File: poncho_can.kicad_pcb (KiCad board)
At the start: 2 copper layers, 85.7 x 60.3 mm, 5 parts

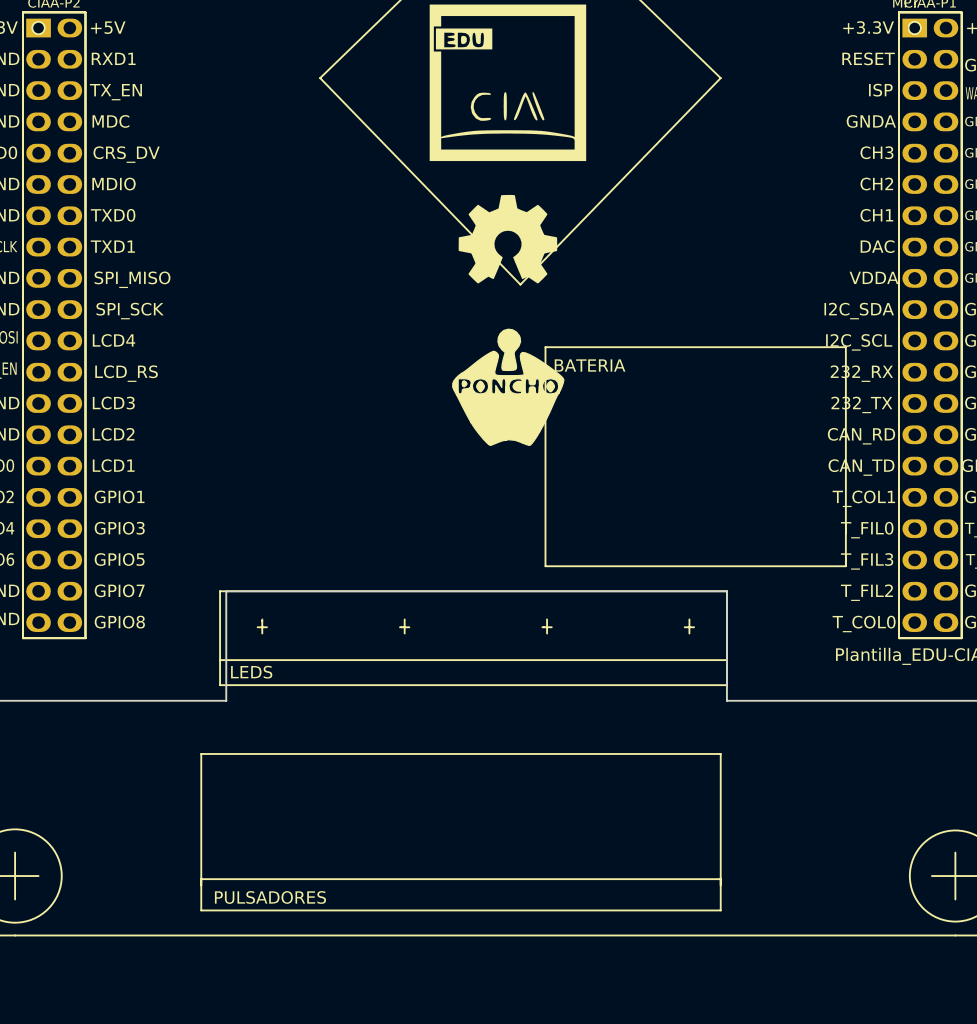
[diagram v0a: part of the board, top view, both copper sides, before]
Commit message: Selección de footprints y ubicacion de componentes
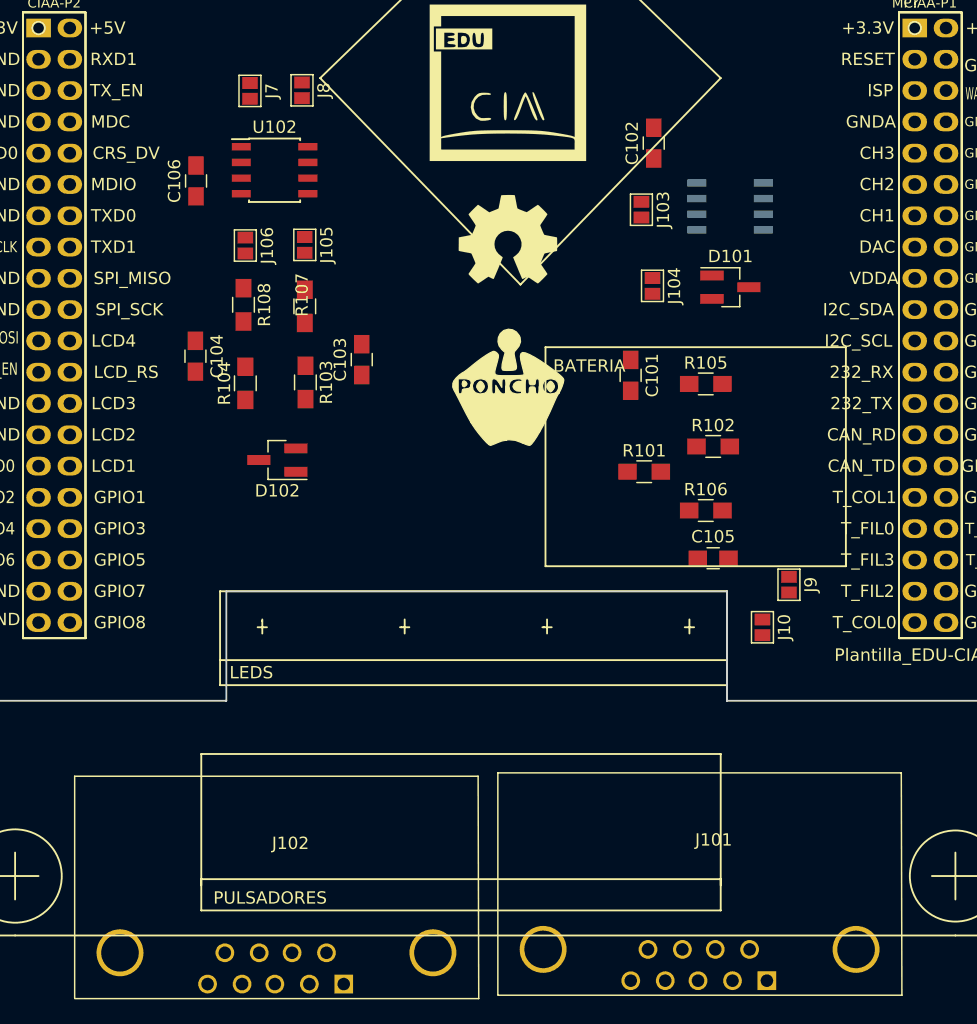
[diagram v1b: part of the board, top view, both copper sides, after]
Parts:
- added C101: 47n, Capacitors_SMD:C_0805_HandSoldering, F.Cu at (114.1, 114.5)
- added C102: 47n, Capacitors_SMD:C_0805_HandSoldering, F.Cu at (116.0, 95.7)
- added C103: 47n, Capacitors_SMD:C_0805_HandSoldering, F.Cu at (92.3, 113.3)
- added C104: 47n, Capacitors_SMD:C_0805_HandSoldering, F.Cu at (78.8, 113.0)
- added C105: 100n, Capacitors_SMD:C_0805_HandSoldering, F.Cu at (120.8, 129.4)
- added C106: 100n, Capacitors_SMD:C_0805_HandSoldering, F.Cu at (78.8, 98.8)
- added D101: RSB27C2, TO_SOT_Packages_SMD:SOT-23_Handsoldering, F.Cu at (122.2, 107.4)
- added D102: RSB27C2, TO_SOT_Packages_SMD:SOT-23_Handsoldering, F.Cu at (85.4, 121.4)
- added J10: GS2, Connect:GS2, F.Cu at (124.8, 135.0)
- added J101: DB9_Male_MountingHoles, Connect:DB9MC, F.Cu at (125.2, 163.7)
- added J102: DB9_Male_MountingHoles, Connect:DB9MC, F.Cu at (90.8, 164.0)
- added J103: GS2, Connect:GS2, F.Cu at (115.0, 101.1)
- added J104: GS2, Connect:GS2, F.Cu at (115.9, 107.3)
- added J105: GS2, Connect:GS2, F.Cu at (87.7, 104.0)
- added J106: GS2, Connect:GS2, F.Cu at (82.8, 104.0)
- added J7: GS2, Connect:GS2, F.Cu at (83.2, 91.5)
- added J8: GS2, Connect:GS2, F.Cu at (87.4, 91.4)
- added J9: GS2, Connect:GS2, F.Cu at (127.0, 131.6)
- added R101: 60, Resistors_SMD:R_0805_HandSoldering, F.Cu at (115.2, 122.4)
- added R102: 60, Resistors_SMD:R_0805_HandSoldering, F.Cu at (120.8, 120.3)
- added R103: 60, Resistors_SMD:R_0805_HandSoldering, F.Cu at (87.7, 115.1)
- added R104: 60, Resistors_SMD:R_0805_HandSoldering, F.Cu at (82.8, 115.2)
- added R105: 60, Resistors_SMD:R_0805_HandSoldering, F.Cu at (120.2, 115.2)
- added R106: 60, Resistors_SMD:R_0805_HandSoldering, F.Cu at (120.2, 125.5)
- added R107: 60, Resistors_SMD:R_0805_HandSoldering, F.Cu at (87.7, 109.0)
- added R108: 60, Resistors_SMD:R_0805_HandSoldering, F.Cu at (82.7, 108.8)
- added U101: TJA1051T, Housings_SOIC:SOIC-8_3.9x4.9mm_Pitch1.27mm, B.Cu at (122.2, 100.8)
- added U102: TJA1051T, Housings_SOIC:SOIC-8_3.9x4.9mm_Pitch1.27mm, F.Cu at (85.2, 97.9)
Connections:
- XA101 pad 1: +3.3VP -> +3V3
- XA101 pad 42: +5V -> +5VP
- XA101 pad 43: GND -> GNDD
- XA101 pad 45: GND -> GNDD
- XA101 pad 47: GND -> GNDD
- XA101 pad 51: GND -> GNDD
- XA101 pad 53: GND -> GNDD
- XA101 pad 57: GND -> GNDD
- XA101 pad 59: GND -> GNDD
- XA101 pad 65: GND -> GNDD
- XA101 pad 67: GND -> GNDD
- XA101 pad 77: GND -> GNDD
- XA101 pad 79: GND -> GNDD

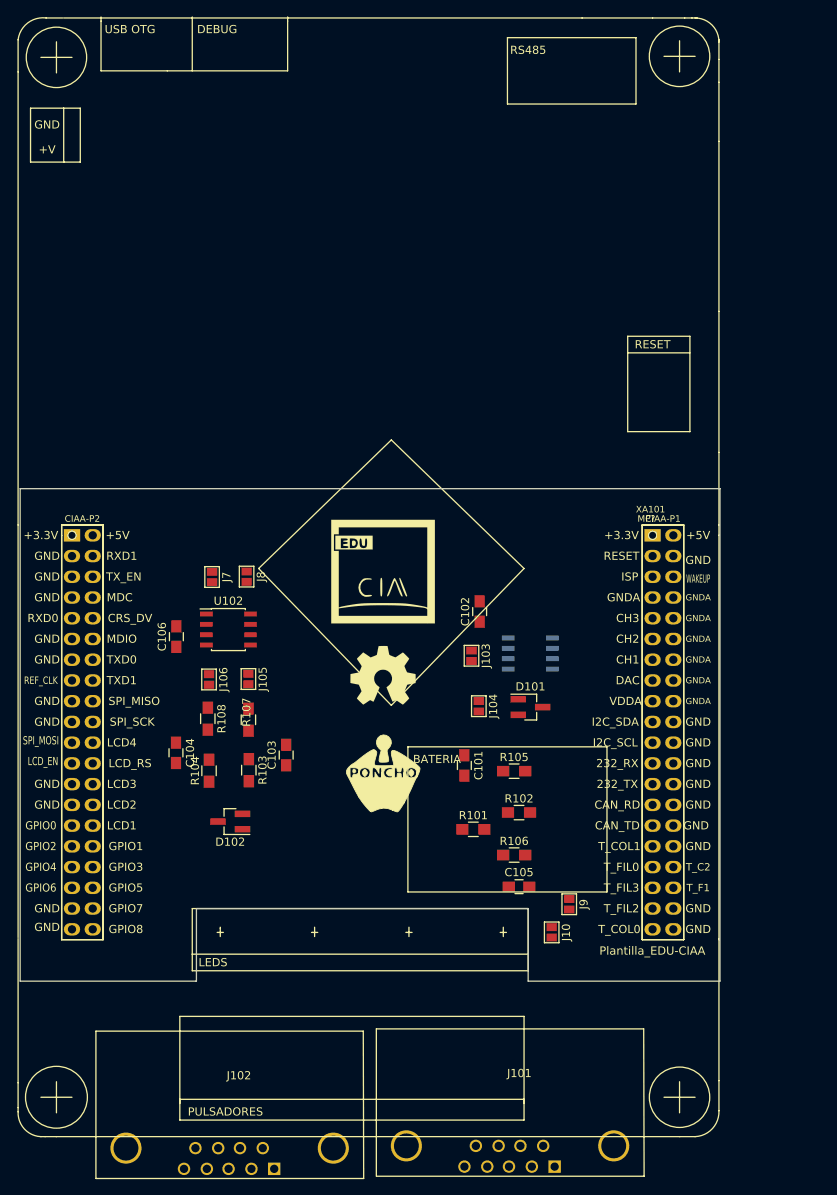
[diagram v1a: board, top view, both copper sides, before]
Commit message: Ruteada una mitad.
Falta cambiar el tamaño de la placa.
Verificar las distancias.
Hacer el cooper pour
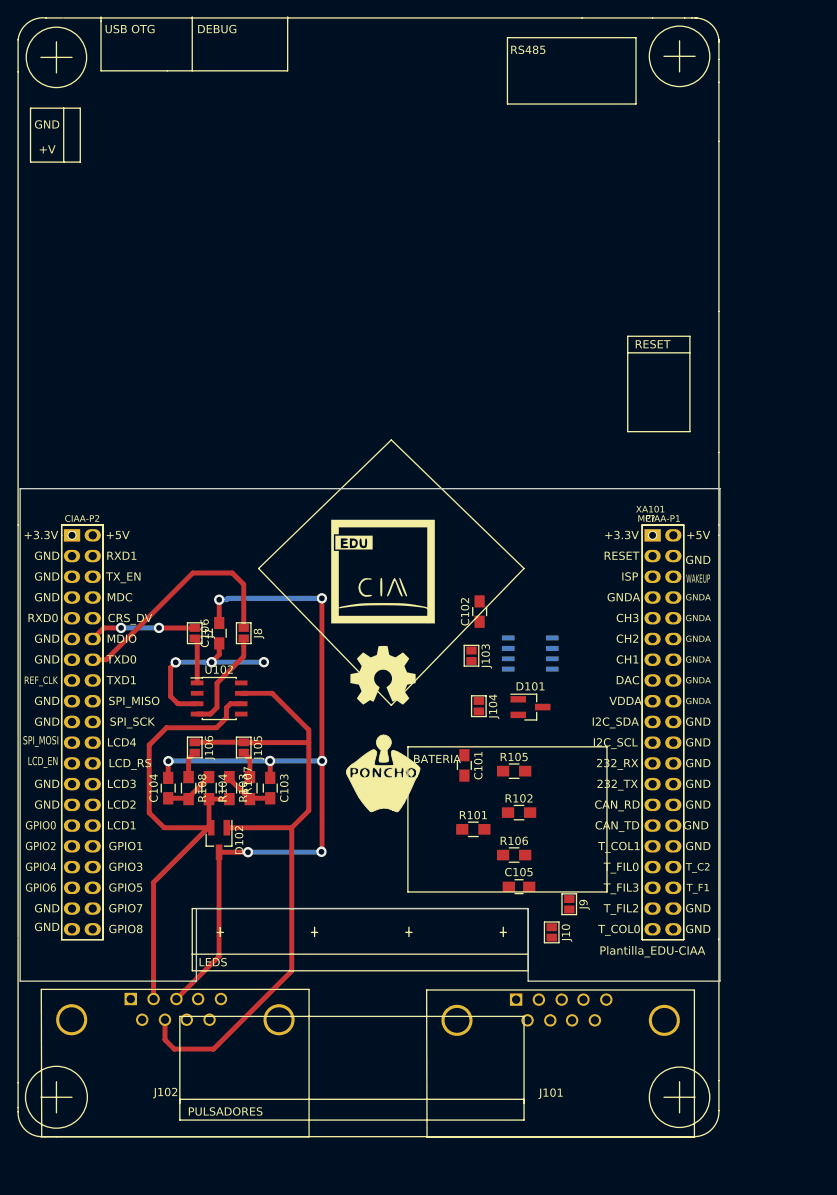
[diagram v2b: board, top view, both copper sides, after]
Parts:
- moved J102 27.2 mm to (73.2, 143.2), turned to 180 degrees
- moved J101 21.0 mm to (120.4, 143.2), turned to 180 degrees
- moved R108 8.82 mm to (80.3, 117.3)
- moved U102 8.52 mm to (84.1, 106.3)
- moved J106 8.52 mm to (81.1, 112.3)
- moved J105 8.40 mm to (87.1, 112.3)
- moved R107 8.38 mm to (87.8, 117.3)
- moved J7 7.21 mm to (81.1, 98.3)
- moved J8 6.94 mm to (87.1, 98.3)
- moved C106 5.27 mm to (84.1, 98.3)
- moved C103 4.49 mm to (90.3, 117.3), turned to 270 degrees
- moved C104 4.43 mm to (77.8, 117.3), turned to 90 degrees
- moved R103 3.24 mm to (85.3, 117.3)
- moved D102 2.64 mm to (84.0, 123.7), turned to 270 degrees
- moved R104 2.12 mm to (82.8, 117.3), turned to 270 degrees
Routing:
- net GND: track 0.00 -> 102.3 mm, vias 0 -> 7
- net Net-(D102-Pad1): track 0.00 -> 85.3 mm
- net Net-(D102-Pad2): track 0.00 -> 61.0 mm
- net Net-(J8-Pad1): track 0.00 -> 28.8 mm
- net +5V: track 0.00 -> 21.6 mm, vias 0 -> 3
- net Net-(J7-Pad1): track 0.00 -> 13.1 mm, vias 0 -> 2
- net Net-(J8-Pad2): track 0.00 -> 12.6 mm
- net Net-(C103-Pad2): track 0.00 -> 6.28 mm
- net Net-(C104-Pad1): track 0.00 -> 6.28 mm
- net Net-(J7-Pad2): track 0.00 -> 5.58 mm
- net Net-(J106-Pad2): track 0.00 -> 3.30 mm
- net Net-(J105-Pad2): track 0.00 -> 3.30 mm
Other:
- net class Default: clearance 0.51 -> 0.4; trace_width 0.381 -> 0.4; via_dia 0.6 -> 1.27; via_drill 0.4 -> 0.7
- rule trace_clearance: 0.51 -> 0.4
- rule trace_min: 0.2 -> 0.4

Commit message: Improved PCB
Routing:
- net GND: track 102.3 -> 125.6 mm, vias 7 -> 9
- net Net-(J8-Pad1): track 28.8 -> 32.1 mm
- net +5V: track 21.6 -> 23.0 mm
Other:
- net class Default: trace_width 0.4 -> 0.6
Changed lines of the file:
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@@
   (general
     (links 77)
-    (no_connects 61)
-    (area 17.572141 15.774999 279.500001 169.160001)
+    (no_connects 53)
+    (area 17.572141 15.774999 279.500001 169.310001)
     (thickness 1.6)
     (drawings 35)
-    (tracks 101)
+    (tracks 111)
     (zones 0)
     (modules 33)
@@
   (net_class Default "This is the default net class."
     (clearance 0.4)
-    (trace_width 0.4)
+    (trace_width 0.6)
     (via_dia 1.27)
     (via_drill 0.7)
@@
     (effects (font (size 1.5 1.5) (thickness 0.3)))
   )
+  (segment (start 83.15 101.9) (end 77.825 101.9) (width 0.6) (layer B.Cu) (net 1))
+  (segment (start 78.235 106.985) (end 81.375 106.985) (width 0.6) (layer F.Cu) (net 1))
+  (segment (start 77.625 106.375) (end 78.235 106.985) (width 0.6) (layer F.Cu) (net 1))
+  (segment (start 77.625 102.075) (end 77.625 106.375) (width 0.6) (layer F.Cu) (net 1))
+  (segment (start 77.7 102) (end 77.625 102.075) (width 0.6) (layer F.Cu) (net 1))
+  (segment (start 77.7 102.025) (end 77.7 102) (width 0.6) (layer F.Cu) (net 1))
+  (via (at 77.7 102.025) (size 1.27) (drill 0.7) (layers F.Cu B.Cu) (net 1))
+  (segment (start 77.825 101.9) (end 77.7 102.025) (width 0.6) (layer B.Cu) (net 1))
   (segment (start 83.15 101.9) (end 89.55 101.9) (width 0.6) (layer B.Cu) (net 1))
   (via (at 89.55 101.9) (size 1.27) (drill 0.7) (layers F.Cu B.Cu) (net 1))
-  (segment (start 78.115001 106.090001) (end 79.01 106.985) (width 0.6) (layer F.Cu) (net 1))
-  (segment (start 79.01 106.985) (end 81.375 106.985) (width 0.6) (layer F.Cu) (net 1))
-  (segment (start 78.75 101.925) (end 78.115001 102.559999) (width 0.6) (layer F.Cu) (net 1))
-  (segment (start 78.115001 102.559999) (end 78.115001 106.090001) (width 0.6) (layer F.Cu) (net 1))
-  (segment (start 82.251975 101.9) (end 78.775 101.9) (width 0.6) (layer B.Cu) (net 1))
-  (segment (start 78.775 101.9) (end 78.75 101.925) (width 0.6) (layer B.Cu) (net 1))
-  (via (at 78.75 101.925) (size 1.27) (drill 0.7) (layers F.Cu B.Cu) (net 1))
-  (segment (start 83.15 101.9) (end 82.251975 101.9) (width 0.6) (layer B.Cu) (net 1))
   (segment (start 84.075 99.6) (end 84.075 100.975) (width 0.6) (layer F.Cu) (net 1))
   (segment (start 84.075 100.975) (end 83.15 101.9) (width 0.6) (layer F.Cu) (net 1))
   (via (at 83.15 101.9) (size 1.27) (drill 0.7) (layers F.Cu B.Cu) (net 1))
-  (segment (start 96.65 94.075) (end 96.65 113.975) (width 0.6) (layer F.Cu) (net 2))
+  (segment (start 84.075 94.25) (end 96.725 94.25) (width 0.6) (layer B.Cu) (net 2))
+  (segment (start 96.725 94.25) (end 96.65 113.975) (width 0.6) (layer F.Cu) (net 2))
+  (via (at 84.075 94.25) (size 1.27) (drill 0.7) (layers F.Cu B.Cu) (net 2))
+  (via (at 96.725 94.25) (size 1.27) (drill 0.7) (layers F.Cu B.Cu) (net 2))
   (segment (start 96.65 113.975) (end 96.675 114) (width 0.6) (layer F.Cu) (net 2))
-  (segment (start 85.148025 94.075) (end 96.65 94.075) (width 0.6) (layer B.Cu) (net 2))
-  (via (at 96.65 94.075) (size 1.27) (drill 0.7) (layers F.Cu B.Cu) (net 2))
-  (segment (start 84.075 94.25) (end 84.973025 94.25) (width 0.6) (layer B.Cu) (net 2))
-  (segment (start 84.973025 94.25) (end 85.148025 94.075) (width 0.6) (layer B.Cu) (net 2))
+  (segment (start 76.1 105.575) (end 76.1 96.175) (width 0.6) (layer F.Cu) (net 2))
+  (segment (start 79.627976 105.715) (end 79.493988 105.581012) (width 0.4) (layer F.Cu) (net 2))
+  (via (at 79.493988 105.581012) (size 1.27) (drill 0.7) (layers F.Cu B.Cu) (net 2))
+  (segment (start 81.375 105.715) (end 79.627976 105.715) (width 0.4) (layer F.Cu) (net 2))
+  (segment (start 78.595963 105.581012) (end 78.589951 105.575) (width 0.4) (layer B.Cu) (net 2))
+  (segment (start 79.493988 105.581012) (end 78.595963 105.581012) (width 0.4) (layer B.Cu) (net 2))
+  (via (at 76.1 105.575) (size 1.27) (drill 0.7) (layers F.Cu B.Cu) (net 2))
+  (segment (start 78.589951 105.575) (end 76.1 105.575) (width 0.4) (layer B.Cu) (net 2))
+  (segment (start 78.025 94.25) (end 84.075 94.25) (width 0.6) (layer F.Cu) (net 2))
+  (segment (start 76.1 96.175) (end 78.025 94.25) (width 0.6) (layer F.Cu) (net 2))
   (segment (start 84.075 97.1) (end 84.075 94.25) (width 0.6) (layer F.Cu) (net 2))
-  (via (at 84.075 94.25) (size 1.27) (drill 0.7) (layers F.Cu B.Cu) (net 2))
   (segment (start 96.675 114) (end 96.675 125.05) (width 0.6) (layer F.Cu) (net 2))
   (segment (start 96.675 125.05) (end 96.6 125.125) (width 0.6) (layer F.Cu) (net 2))
@@
   (segment (start 69.94 97.7) (end 68.58 99.06) (width 0.6) (layer F.Cu) (net 57))
   (via (at 72.05 97.7) (size 1.27) (drill 0.7) (layers F.Cu B.Cu) (net 57))
-  (segment (start 76.7 97.7) (end 72.05 97.7) (width 0.6) (layer B.Cu) (net 57))
-  (segment (start 81.075 97.71) (end 76.71 97.71) (width 0.6) (layer F.Cu) (net 57))
-  (segment (start 76.71 97.71) (end 76.7 97.7) (width 0.6) (layer F.Cu) (net 57))
-  (via (at 76.7 97.7) (size 1.27) (drill 0.7) (layers F.Cu B.Cu) (net 57))
+  (segment (start 78.575 97.725) (end 72.05 97.7) (width 0.6) (layer B.Cu) (net 57))
+  (segment (start 81.075 97.71) (end 78.585 97.735) (width 0.6) (layer F.Cu) (net 57))
+  (segment (start 78.585 97.735) (end 78.575 97.725) (width 0.6) (layer F.Cu) (net 57))
+  (via (at 78.575 97.725) (size 1.27) (drill 0.7) (layers F.Cu B.Cu) (net 57))
   (segment (start 81.375 104.445) (end 81.375 99.29) (width 0.6) (layer F.Cu) (net 58))
   (segment (start 81.375 99.29) (end 81.075 98.99) (width 0.6) (layer F.Cu) (net 58))
-  (segment (start 80.85 90.975) (end 70.225 101.6) (width 0.6) (layer F.Cu) (net 59))
-  (segment (start 70.225 101.6) (end 68.58 101.6) (width 0.6) (layer F.Cu) (net 59))
-  (segment (start 85.675 90.975) (end 80.85 90.975) (width 0.6) (layer F.Cu) (net 59))
-  (segment (start 87.075 92.375) (end 85.675 90.975) (width 0.6) (layer F.Cu) (net 59))
-  (segment (start 87.075 97.71) (end 87.075 92.375) (width 0.6) (layer F.Cu) (net 59))
+  (segment (start 87.075 97.71) (end 87.075 92.45) (width 0.6) (layer F.Cu) (net 59))
+  (segment (start 73.05 101.6) (end 68.58 101.6) (width 0.6) (layer F.Cu) (net 59))
+  (segment (start 74.6 100.05) (end 73.05 101.6) (width 0.6) (layer F.Cu) (net 59))
+  (segment (start 74.6 94.025) (end 74.6 100.05) (width 0.6) (layer F.Cu) (net 59))
+  (segment (start 77.375 91.25) (end 74.6 94.025) (width 0.6) (layer F.Cu) (net 59))
+  (segment (start 85.875 91.25) (end 77.375 91.25) (width 0.6) (layer F.Cu) (net 59))
+  (segment (start 87.075 92.45) (end 85.875 91.25) (width 0.6) (layer F.Cu) (net 59))
   (segment (start 87.075 98.99) (end 87.075 101.2) (width 0.6) (layer F.Cu) (net 60))
   (segment (start 82.995 108.255) (end 81.375 108.255) (width 0.6) (layer F.Cu) (net 60))
